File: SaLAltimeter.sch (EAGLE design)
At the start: 83 parts, among them U1 ATSAMD21G-A, U2 V_REG_LDOSMD, U3 ADXL345, Y3 32MHz

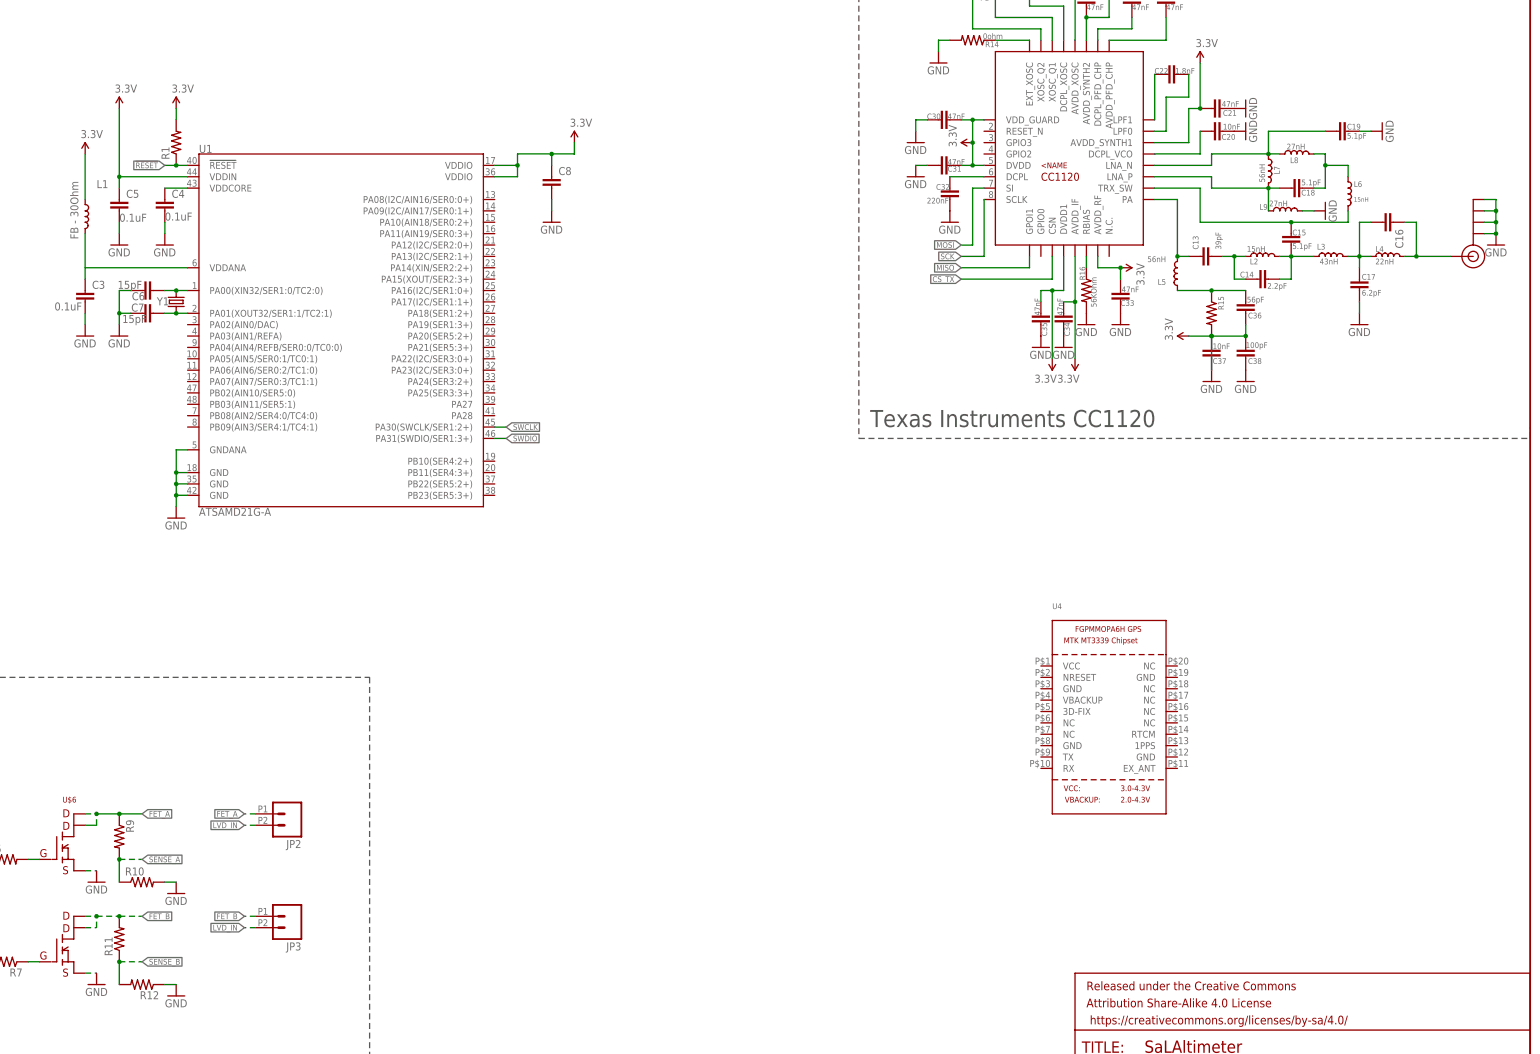
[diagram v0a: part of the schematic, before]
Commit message: fixed gps
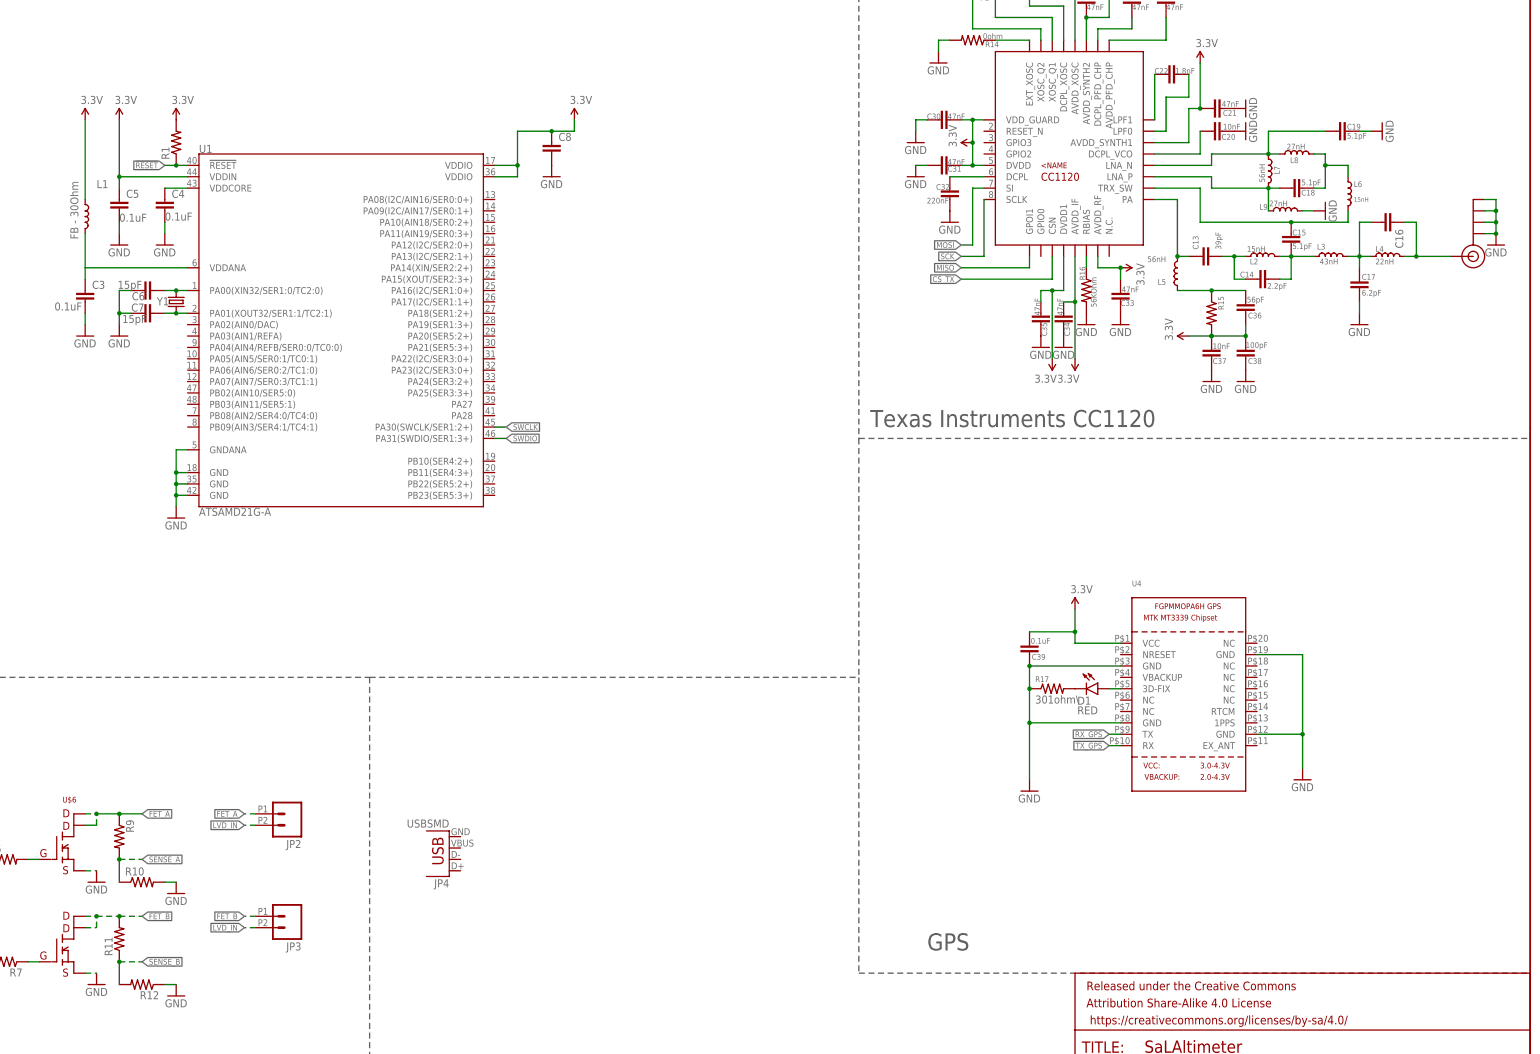
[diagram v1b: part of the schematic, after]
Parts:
- added C39: 0.1uF, SparkFun-Capacitors:CAP0402-CAP
- added D1: RED, SparkFun-LED:LED-RED0603
- added JP4: USBSMD, SparkFun-Connectors:USBSMD
- added R17: 301ohm\, SparkFun-Passives:RESISTOR0402-RES
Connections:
- new net N$30: D1.C, R17.2
- new net N$31: D1.A, U4.3D-FIX
- new net RX_GPS: U4.TX
- new net TX_GPS: U4.RX
- net 3.3V: now also C39.2, U4.VCC
- net GND: now also C39.1, R17.1, U4.GND@1, U4.GND@2, U4.GND@3, U4.GND@4
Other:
- note added: "GPS"
- moved on the sheet: C8, U4
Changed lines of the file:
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@@
 <part name="GND44" library="SparkFun-Aesthetics" deviceset="GND" device=""/>
 <part name="U4" library="adafruit" deviceset="GPS_FGPMMOPA6H" device=""/>
+<part name="GND45" library="SparkFun-Aesthetics" deviceset="GND" device=""/>
+<part name="D1" library="SparkFun-LED" deviceset="LED-RED" device="0603" value="RED"/>
+<part name="R17" library="SparkFun-Passives" deviceset="RESISTOR" device="0402-RES" value="301ohm\"/>
+<part name="C39" library="SparkFun-Capacitors" deviceset="CAP" device="0402-CAP" value="0.1uF"/>
+<part name="SUPPLY22" library="SparkFun-Aesthetics" deviceset="3.3V" device=""/>
+<part name="GND46" library="SparkFun-Aesthetics" deviceset="GND" device=""/>
+<part name="JP4" library="SparkFun-Connectors" deviceset="USB" device="SMD"/>
 </parts>
 <sheets>
@@
 <wire x1="172.72" y1="101.6" x2="172.72" y2="0" width="0.1524" layer="97" style="longdash"/>
 <text x="60.96" y="7.62" size="3.81" layer="97">Firing circuit</text>
+<wire x1="281.94" y1="154.94" x2="281.94" y2="101.6" width="0.1524" layer="97" style="longdash"/>
+<wire x1="281.94" y1="101.6" x2="281.94" y2="35.56" width="0.1524" layer="97" style="longdash"/>
+<wire x1="281.94" y1="35.56" x2="431.8" y2="35.56" width="0.1524" layer="97" style="longdash"/>
+<text x="297.18" y="40.64" size="3.81" layer="97">GPS</text>
+<wire x1="172.72" y1="101.6" x2="281.94" y2="101.6" width="0.1524" layer="97" style="longdash"/>
 </plain>
 <instances>
@@
 <attribute name="VALUE" x="122.936" y="182.499" size="1.778" layer="96" rot="R180"/>
 </instance>
-<instance part="C8" gate="G$1" x="213.36" y="210.82"/>
+<instance part="C8" gate="G$1" x="213.36" y="218.44"/>
 <instance part="Y1" gate="G$1" x="129.54" y="185.42" smashed="yes" rot="R90">
 <attribute name="NAME" x="125.222" y="184.658" size="1.778" layer="95"/>
@@
 <instance part="GND7" gate="1" x="127" y="198.12"/>
 <instance part="R1" gate="G$1" x="129.54" y="220.98" rot="R90"/>
-<instance part="SUPPLY2" gate="G$1" x="129.54" y="228.6"/>
-<instance part="SUPPLY3" gate="G$1" x="116.84" y="228.6"/>
-<instance part="SUPPLY4" gate="G$1" x="109.22" y="218.44"/>
+<instance part="SUPPLY2" gate="G$1" x="129.54" y="226.06"/>
+<instance part="SUPPLY3" gate="G$1" x="116.84" y="226.06"/>
+<instance part="SUPPLY4" gate="G$1" x="109.22" y="226.06"/>
 <instance part="GND8" gate="1" x="109.22" y="177.8"/>
-<instance part="SUPPLY5" gate="G$1" x="218.44" y="220.98"/>
-<instance part="GND9" gate="1" x="213.36" y="203.2"/>
+<instance part="SUPPLY5" gate="G$1" x="218.44" y="226.06"/>
+<instance part="GND9" gate="1" x="213.36" y="213.36"/>
 <instance part="GND10" gate="1" x="129.54" y="137.16"/>
 <instance part="JP1" gate="G$1" x="25.4" y="175.26"/>
@@
 <instance part="J$1" gate="1" x="419.1" y="195.58" rot="R180"/>
 <instance part="GND44" gate="1" x="424.18" y="198.12"/>
-<instance part="U4" gate="G$1" x="337.82" y="93.98"/>
+<instance part="U4" gate="G$1" x="355.6" y="99.06"/>
+<instance part="GND45" gate="1" x="381" y="78.74"/>
+<instance part="D1" gate="G$1" x="335.28" y="99.06" rot="R270"/>
+<instance part="R17" gate="G$1" x="325.12" y="99.06" smashed="yes">
+<attribute name="NAME" x="321.31" y="100.5586" size="1.27" layer="95"/>
+<attribute name="VALUE" x="321.31" y="95.758" size="1.778" layer="96"/>
+</instance>
+<instance part="C39" gate="G$1" x="320.04" y="109.22" smashed="yes" rot="R180">
+<attribute name="NAME" x="320.548" y="105.537" size="1.27" layer="95"/>
+<attribute name="VALUE" x="320.294" y="109.093" size="1.27" layer="96"/>
+</instance>
+<instance part="SUPPLY22" gate="G$1" x="330.2" y="116.84"/>
+<instance part="GND46" gate="1" x="320.04" y="76.2"/>
+<instance part="JP4" gate="G$1" x="190.5" y="66.04" rot="R180"/>
 </instances>
 <busses>
@@
 <pinref part="R1" gate="G$1" pin="2"/>
 <pinref part="SUPPLY2" gate="G$1" pin="3.3V"/>
-<wire x1="129.54" y1="228.6" x2="129.54" y2="226.06" width="0.1524" layer="91"/>
 </segment>
 <segment>
@@
 <wire x1="132.08" y1="213.36" x2="116.84" y2="213.36" width="0.1524" layer="91"/>
 <wire x1="116.84" y1="213.36" x2="116.84" y2="210.82" width="0.1524" layer="91"/>
-<wire x1="116.84" y1="213.36" x2="116.84" y2="228.6" width="0.1524" layer="91"/>
+<wire x1="116.84" y1="213.36" x2="116.84" y2="226.06" width="0.1524" layer="91"/>
 <junction x="116.84" y="213.36"/>
 <pinref part="SUPPLY3" gate="G$1" pin="3.3V"/>
@@
 <pinref part="L1" gate="G$1" pin="1"/>
 <pinref part="SUPPLY4" gate="G$1" pin="3.3V"/>
-<wire x1="109.22" y1="218.44" x2="109.22" y2="208.28" width="0.1524" layer="91"/>
+<wire x1="109.22" y1="226.06" x2="109.22" y2="208.28" width="0.1524" layer="91"/>
 </segment>
 <segment>
@@
 <wire x1="205.74" y1="213.36" x2="205.74" y2="215.9" width="0.1524" layer="91"/>
 <pinref part="C8" gate="G$1" pin="1"/>
-<wire x1="205.74" y1="215.9" x2="205.74" y2="218.44" width="0.1524" layer="91"/>
-<wire x1="205.74" y1="218.44" x2="213.36" y2="218.44" width="0.1524" layer="91"/>
-<wire x1="213.36" y1="218.44" x2="213.36" y2="215.9" width="0.1524" layer="91"/>
+<wire x1="205.74" y1="215.9" x2="205.74" y2="223.52" width="0.1524" layer="91"/>
+<wire x1="205.74" y1="223.52" x2="213.36" y2="223.52" width="0.1524" layer="91"/>
 <junction x="205.74" y="215.9"/>
-<wire x1="213.36" y1="218.44" x2="218.44" y2="218.44" width="0.1524" layer="91"/>
-<wire x1="218.44" y1="218.44" x2="218.44" y2="220.98" width="0.1524" layer="91"/>
-<junction x="213.36" y="218.44"/>
+<wire x1="213.36" y1="223.52" x2="218.44" y2="223.52" width="0.1524" layer="91"/>
+<wire x1="218.44" y1="223.52" x2="218.44" y2="226.06" width="0.1524" layer="91"/>
+<junction x="213.36" y="223.52"/>
 <pinref part="SUPPLY5" gate="G$1" pin="3.3V"/>
 </segment>
@@
 <wire x1="368.3" y1="180.34" x2="368.3" y2="177.8" width="0.1524" layer="91"/>
 <pinref part="R15" gate="G$1" pin="2"/>
-<wire x1="360.68" y1="177.8" x2="360.68" y2="170.18" width="0.1524" layer="91"/>
 <wire x1="368.3" y1="177.8" x2="360.68" y2="177.8" width="0.1524" layer="91"/>
 <junction x="360.68" y="177.8"/>
@@
 <wire x1="322.58" y1="187.96" x2="322.58" y2="185.42" width="0.1524" layer="91"/>
 <junction x="325.12" y="187.96"/>
+</segment>
+<segment>
+<pinref part="U4" gate="G$1" pin="VCC"/>
+<wire x1="340.36" y1="109.22" x2="330.2" y2="109.22" width="0.1524" layer="91"/>
+<wire x1="330.2" y1="109.22" x2="330.2" y2="111.76" width="0.1524" layer="91"/>
+<pinref part="C39" gate="G$1" pin="2"/>
+<wire x1="330.2" y1="111.76" x2="330.2" y2="116.84" width="0.1524" layer="91"/>
+<wire x1="330.2" y1="111.76" x2="320.04" y2="111.76" width="0.1524" layer="91"/>
+<junction x="330.2" y="111.76"/>
+<pinref part="SUPPLY22" gate="G$1" pin="3.3V"/>
 </segment>
 </net>
@@
 <pinref part="C8" gate="G$1" pin="2"/>
 <pinref part="GND9" gate="1" pin="GND"/>
-<wire x1="213.36" y1="205.74" x2="213.36" y2="208.28" width="0.1524" layer="91"/>
 </segment>
 <segment>
@@
 <junction x="424.18" y="200.66"/>
 </segment>
+<segment>
+<pinref part="U4" gate="G$1" pin="GND@3"/>
+<pinref part="GND45" gate="1" pin="GND"/>
+<wire x1="370.84" y1="88.9" x2="381" y2="88.9" width="0.1524" layer="91"/>
+<wire x1="381" y1="88.9" x2="381" y2="81.28" width="0.1524" layer="91"/>
+<pinref part="U4" gate="G$1" pin="GND@4"/>
+<wire x1="370.84" y1="106.68" x2="381" y2="106.68" width="0.1524" layer="91"/>
+<wire x1="381" y1="106.68" x2="381" y2="88.9" width="0.1524" layer="91"/>
+<junction x="381" y="88.9"/>
+</segment>
+<segment>
+<pinref part="U4" gate="G$1" pin="GND@1"/>
+<wire x1="340.36" y1="104.14" x2="320.04" y2="104.14" width="0.1524" layer="91"/>
+<wire x1="320.04" y1="104.14" x2="320.04" y2="99.06" width="0.1524" layer="91"/>
+<pinref part="U4" gate="G$1" pin="GND@2"/>
+<wire x1="320.04" y1="99.06" x2="320.04" y2="91.44" width="0.1524" layer="91"/>
+<wire x1="320.04" y1="91.44" x2="320.04" y2="78.74" width="0.1524" layer="91"/>
+<wire x1="340.36" y1="91.44" x2="320.04" y2="91.44" width="0.1524" layer="91"/>
+<junction x="320.04" y="91.44"/>
+<pinref part="R17" gate="G$1" pin="1"/>
+<junction x="320.04" y="99.06"/>
+<pinref part="C39" gate="G$1" pin="1"/>
+<junction x="320.04" y="104.14"/>
+<pinref part="GND46" gate="1" pin="GND"/>
+</segment>
 </net>
 <net name="LVD_IN" class="0">
@@
 </segment>
 </net>
+<net name="N$30" class="0">
+<segment>
+<pinref part="D1" gate="G$1" pin="C"/>
+<pinref part="R17" gate="G$1" pin="2"/>
+</segment>
+</net>
+<net name="N$31" class="0">
+<segment>
+<pinref part="U4" gate="G$1" pin="3D-FIX"/>
+<pinref part="D1" gate="G$1" pin="A"/>
+<wire x1="337.82" y1="99.06" x2="340.36" y2="99.06" width="0.1524" layer="91"/>
+</segment>
+</net>
+<net name="RX_GPS" class="0">
+<segment>
+<pinref part="U4" gate="G$1" pin="TX"/>
+<wire x1="340.36" y1="88.9" x2="337.82" y2="88.9" width="0.1524" layer="91"/>
+<label x="337.82" y="88.9" size="1.27" layer="95" rot="R180" xref="yes"/>
+</segment>
+</net>
+<net name="TX_GPS" class="0">
+<segment>
+<pinref part="U4" gate="G$1" pin="RX"/>
+<wire x1="340.36" y1="86.36" x2="337.82" y2="86.36" width="0.1524" layer="91"/>
+<label x="337.82" y="86.36" size="1.27" layer="95" rot="R180" xref="yes"/>
+</segment>
+</net>
